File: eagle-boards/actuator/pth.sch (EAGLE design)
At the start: 12 parts, among them IC1 ULN2003AN, IC2 ULN2003AN

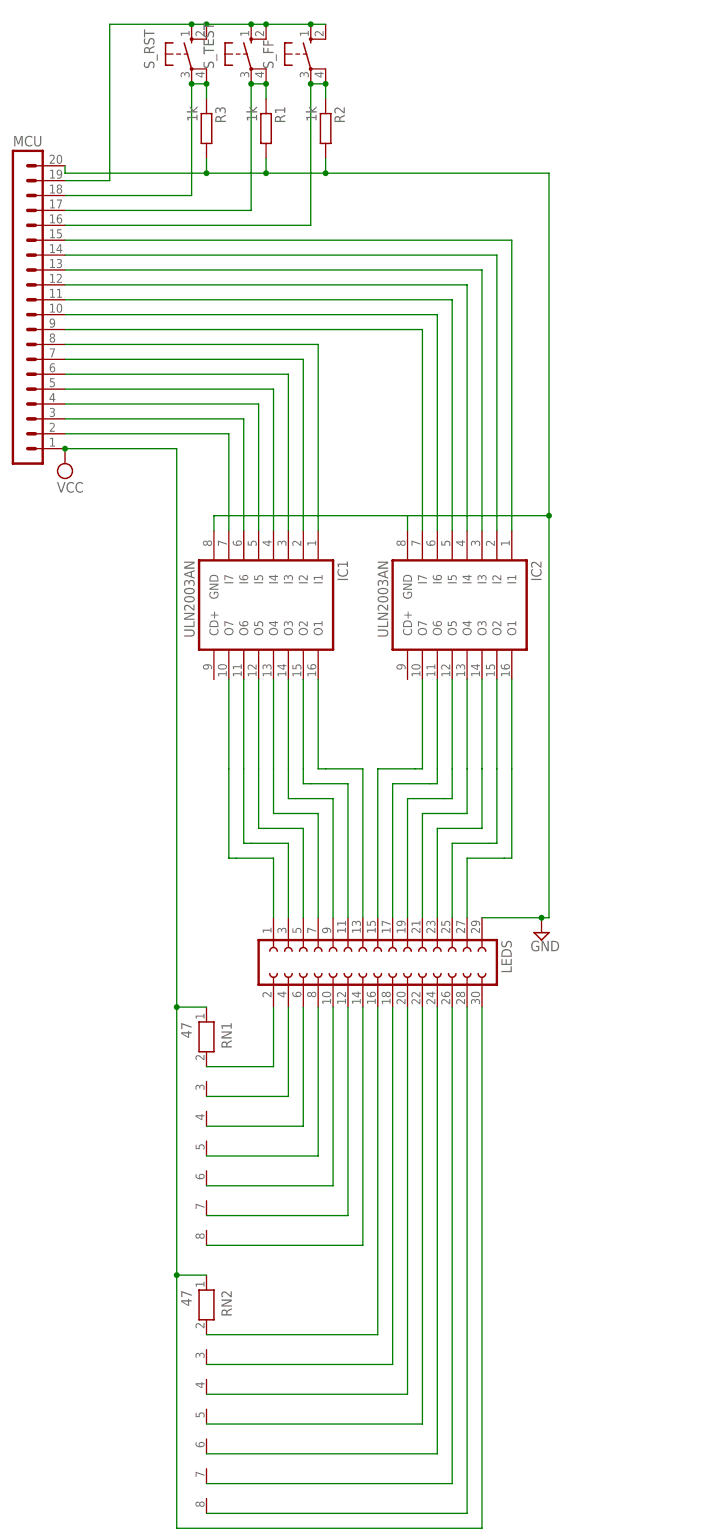
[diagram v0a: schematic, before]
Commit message: Add a new revision for the actuator board.
Rotate the board so that the writing is in the same orientation as the controller board once mounted.

Include +5/GND markings on both connectors.

Put the MCU connector on the _bottom_ layer, rather than the top.
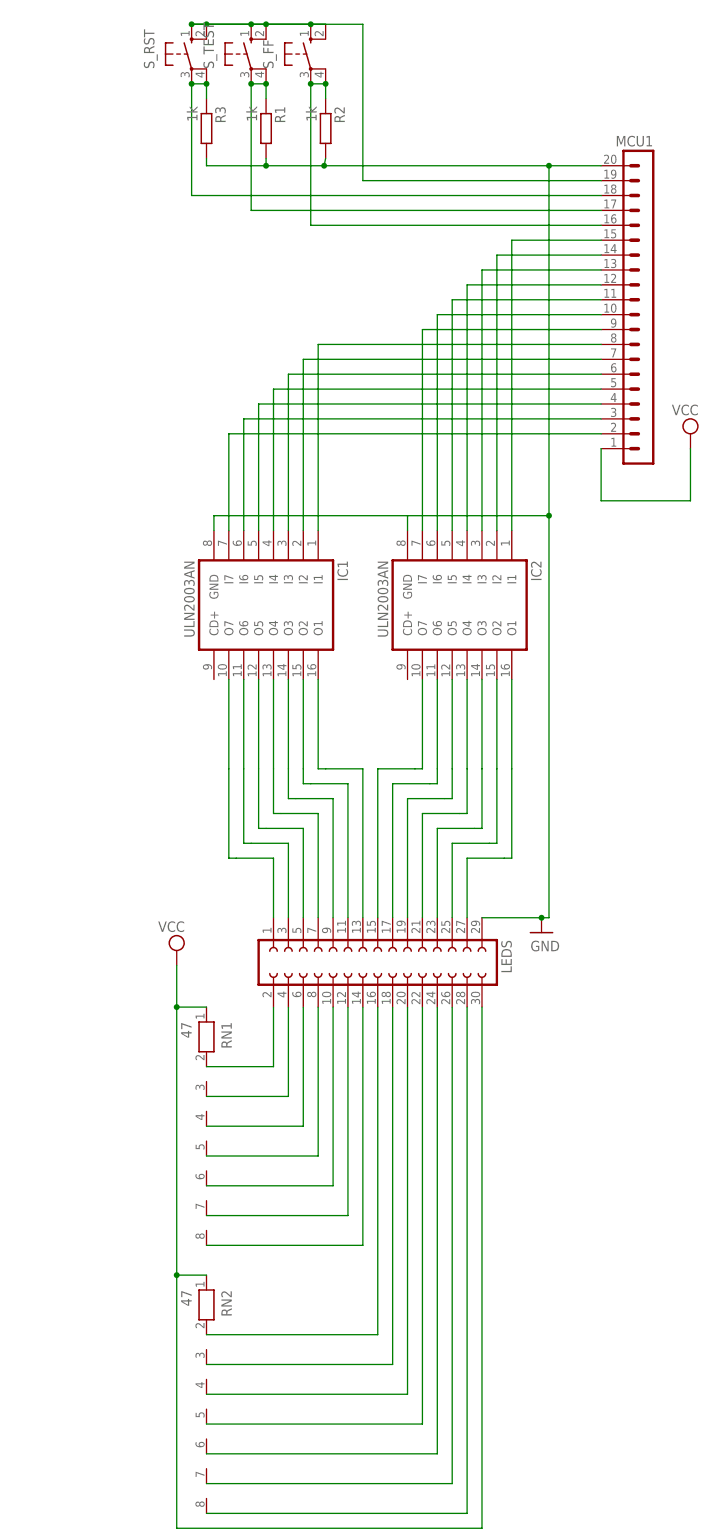
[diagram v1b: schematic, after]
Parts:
- removed MCU: (no value), con-lstb:MA20-1
- added MCU1: (no value), con-lstb:MA20-1
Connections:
- net GND: now also MCU1.20; no longer MCU.20
- net N$1: now also MCU1.8; no longer MCU.8
- net N$10: now also MCU1.10; no longer MCU.10
- net N$11: now also MCU1.11; no longer MCU.11
- net N$12: now also MCU1.12; no longer MCU.12
- net N$13: now also MCU1.13; no longer MCU.13
- net N$14: now also MCU1.14; no longer MCU.14
- net N$15: now also MCU1.15; no longer MCU.15
- net N$17: now also MCU1.18; no longer MCU.18
- net N$18: now also MCU1.17; no longer MCU.17
- net N$19: now also MCU1.16; no longer MCU.16
- net N$2: now also MCU1.19; no longer MCU.19
- net N$3: now also MCU1.2; no longer MCU.2
- net N$4: now also MCU1.3; no longer MCU.3
- net N$5: now also MCU1.4; no longer MCU.4
- net N$6: now also MCU1.5; no longer MCU.5
- net N$7: now also MCU1.6; no longer MCU.6
- net N$8: now also MCU1.7; no longer MCU.7
- net N$9: now also MCU1.9; no longer MCU.9
- net VCC: now also MCU1.1; no longer MCU.1
